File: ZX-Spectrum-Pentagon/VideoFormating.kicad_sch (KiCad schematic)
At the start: 10 parts

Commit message: annotate
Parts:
- gave numbers to parts that had none: 10
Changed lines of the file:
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@@
   (symbol (lib_id "74IEC:74HC574") (at 55.88 38.1 0) (unit 1)
     (in_bom yes) (on_board yes)
-    (property "Reference" "U?" (id 0) (at 55.88 24.13 0))
+    (property "Reference" "U36" (id 0) (at 55.88 24.13 0))
     (property "Value" "74HC574" (id 1) (at 55.88 52.07 0))
     (property "Footprint" "Package_DIP:DIP-20_W7.62mm" (id 2) (at 55.88 45.72 0)
@@
   (symbol (lib_id "74IEC:74HC574") (at 78.74 40.64 0) (unit 1)
     (in_bom yes) (on_board yes)
-    (property "Reference" "U?" (id 0) (at 78.74 26.67 0))
+    (property "Reference" "U37" (id 0) (at 78.74 26.67 0))
     (property "Value" "74HC574" (id 1) (at 78.74 54.61 0))
     (property "Footprint" "Package_DIP:DIP-20_W7.62mm" (id 2) (at 78.74 48.26 0)
@@
   (symbol (lib_id "power:GND") (at 68.58 57.15 0) (unit 1)
     (in_bom yes) (on_board yes)
-    (property "Reference" "#PWR?" (id 0) (at 68.58 63.5 0)
+    (property "Reference" "#PWR053" (id 0) (at 68.58 63.5 0)
       (effects (font (size 1.27 1.27)) hide)
     )
@@
   (symbol (lib_id "74IEC:74HC574") (at 55.88 167.64 0) (unit 1)
     (in_bom yes) (on_board yes)
-    (property "Reference" "U?" (id 0) (at 55.88 153.67 0))
+    (property "Reference" "U41" (id 0) (at 55.88 153.67 0))
     (property "Value" "74HC574" (id 1) (at 55.88 181.61 0))
     (property "Footprint" "Package_DIP:DIP-20_W7.62mm" (id 2) (at 55.88 175.26 0)
@@
   (symbol (lib_id "74IEC:74HC166") (at 82.55 168.91 0) (unit 1)
     (in_bom yes) (on_board yes)
-    (property "Reference" "U?" (id 0) (at 82.55 151.13 0))
+    (property "Reference" "U42" (id 0) (at 82.55 151.13 0))
     (property "Value" "74HC166" (id 1) (at 82.55 186.69 0))
     (property "Footprint" "Package_DIP:DIP-16_W7.62mm" (id 2) (at 82.55 184.15 0)
@@
   (symbol (lib_id "power:GND") (at 71.12 186.69 0) (unit 1)
     (in_bom yes) (on_board yes)
-    (property "Reference" "#PWR?" (id 0) (at 71.12 193.04 0)
+    (property "Reference" "#PWR057" (id 0) (at 71.12 193.04 0)
       (effects (font (size 1.27 1.27)) hide)
     )
@@
   (symbol (lib_id "74IEC:74XX153") (at 135.89 43.18 0) (unit 1)
     (in_bom yes) (on_board yes)
-    (property "Reference" "U?" (id 0) (at 135.89 26.67 0))
+    (property "Reference" "U38" (id 0) (at 135.89 26.67 0))
     (property "Value" "74HC153" (id 1) (at 135.89 59.69 0))
     (property "Footprint" "Package_DIP:DIP-16_W7.62mm" (id 2) (at 135.89 41.91 0)
@@
   (symbol (lib_id "74IEC:74XX153") (at 135.89 88.9 0) (unit 1)
     (in_bom yes) (on_board yes)
-    (property "Reference" "U?" (id 0) (at 135.89 72.39 0))
+    (property "Reference" "U39" (id 0) (at 135.89 72.39 0))
     (property "Value" "74HC153" (id 1) (at 135.89 105.41 0))
     (property "Footprint" "Package_DIP:DIP-16_W7.62mm" (id 2) (at 135.89 87.63 0)
@@
   (symbol (lib_id "power:GND") (at 124.46 125.73 0) (unit 1)
     (in_bom yes) (on_board yes)
-    (property "Reference" "#PWR?" (id 0) (at 124.46 132.08 0)
+    (property "Reference" "#PWR055" (id 0) (at 124.46 132.08 0)
       (effects (font (size 1.27 1.27)) hide)
     )
@@
   (symbol (lib_id "Gal:GAL16V8") (at 83.82 109.22 0) (unit 1)
     (in_bom yes) (on_board yes)
-    (property "Reference" "U?" (id 0) (at 83.82 95.25 0))
+    (property "Reference" "U40" (id 0) (at 83.82 95.25 0))
     (property "Value" "GAL16V8" (id 1) (at 83.82 123.19 0))
     (property "Footprint" "Package_DIP:DIP-20_W7.62mm" (id 2) (at 83.82 95.25 0)
@@
   (symbol (lib_id "zx_custom_symbol:SW_Push_DPDT") (at 114.3 166.37 0) (unit 1)
     (in_bom yes) (on_board yes)
-    (property "Reference" "SWVF?" (id 0) (at 114.3 153.67 0))
+    (property "Reference" "SWVF1" (id 0) (at 114.3 153.67 0))
     (property "Value" "128K/512K" (id 1) (at 114.3 184.15 0))
     (property "Footprint" "ZX-Spectrum-Pentagon:PS-22F03" (id 2) (at 114.3 166.37 0)
@@
   (symbol (lib_id "power:GND") (at 123.19 187.96 0) (mirror y) (unit 1)
     (in_bom yes) (on_board yes)
-    (property "Reference" "#PWR?" (id 0) (at 123.19 194.31 0)
+    (property "Reference" "#PWR058" (id 0) (at 123.19 194.31 0)
       (effects (font (size 1.27 1.27)) hide)
     )
@@
   (symbol (lib_id "Device:R") (at 106.68 153.67 0) (unit 1)
     (in_bom yes) (on_board yes)
-    (property "Reference" "RVF?" (id 0) (at 99.06 151.13 0)
+    (property "Reference" "RVF1" (id 0) (at 99.06 151.13 0)
       (effects (font (size 1.27 1.27)) (justify left))
     )
@@
   (symbol (lib_id "power:VCC") (at 106.68 144.78 0) (unit 1)
     (in_bom yes) (on_board yes)
-    (property "Reference" "#PWR?" (id 0) (at 106.68 148.59 0)
+    (property "Reference" "#PWR056" (id 0) (at 106.68 148.59 0)
       (effects (font (size 1.27 1.27)) hide)
     )
@@
   (symbol (lib_id "74IEC:74HC86") (at 137.16 137.16 0) (unit 4)
     (in_bom yes) (on_board yes)
-    (property "Reference" "U?" (id 0) (at 137.16 133.35 0))
+    (property "Reference" "U9" (id 0) (at 137.16 133.35 0))
     (property "Value" "74HC86" (id 1) (at 137.16 140.97 0))
     (property "Footprint" "Package_DIP:DIP-14_W7.62mm" (id 2) (at 137.16 144.78 0)
@@
   (symbol (lib_id "power:VCC") (at 67.31 120.65 90) (unit 1)
     (in_bom yes) (on_board yes)
-    (property "Reference" "#PWR?" (id 0) (at 71.12 120.65 0)
-      (effects (font (size 1.27 1.27)) hide)
-    )
+    (property "Reference" "#PWR054" (id 0) (at 71.12 120.65 0)
+      (effects (font (size 1.27 1.27)) hide)
+    )

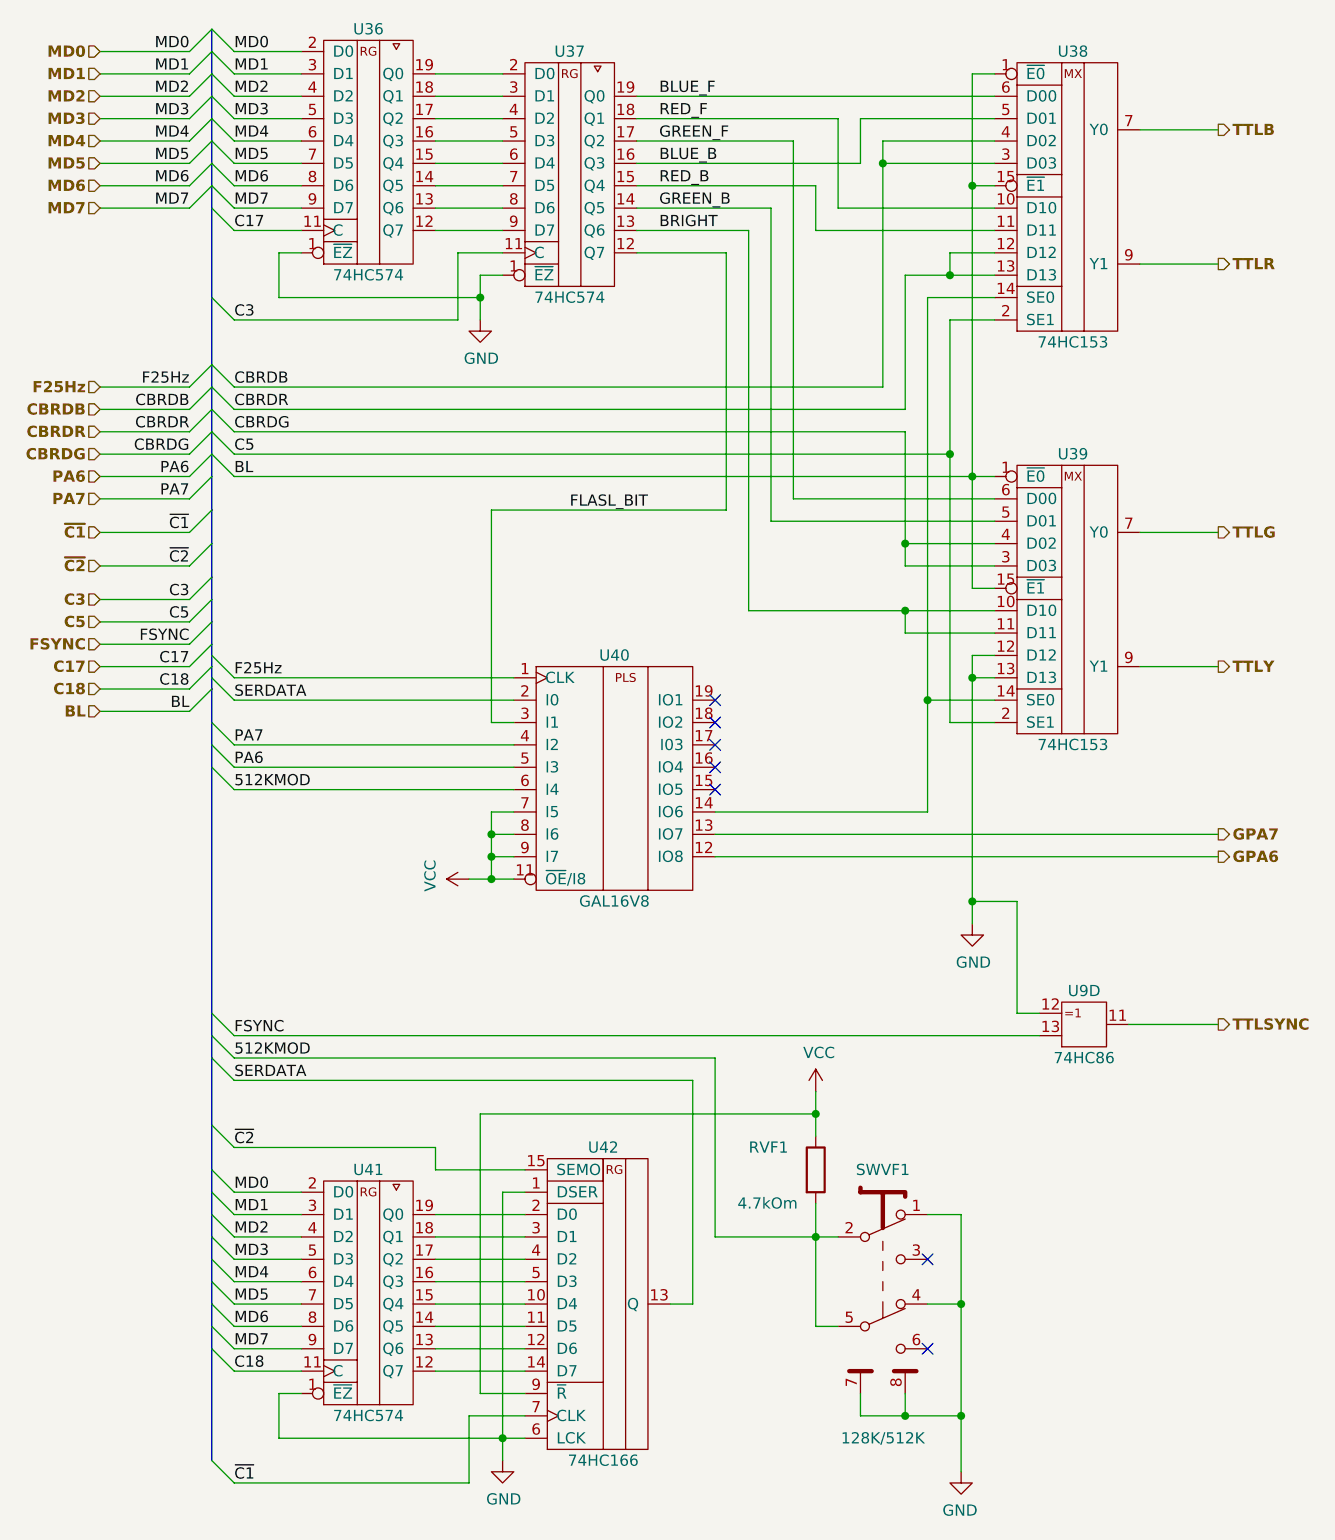
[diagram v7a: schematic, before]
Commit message: delete unuser labels fix problem with units
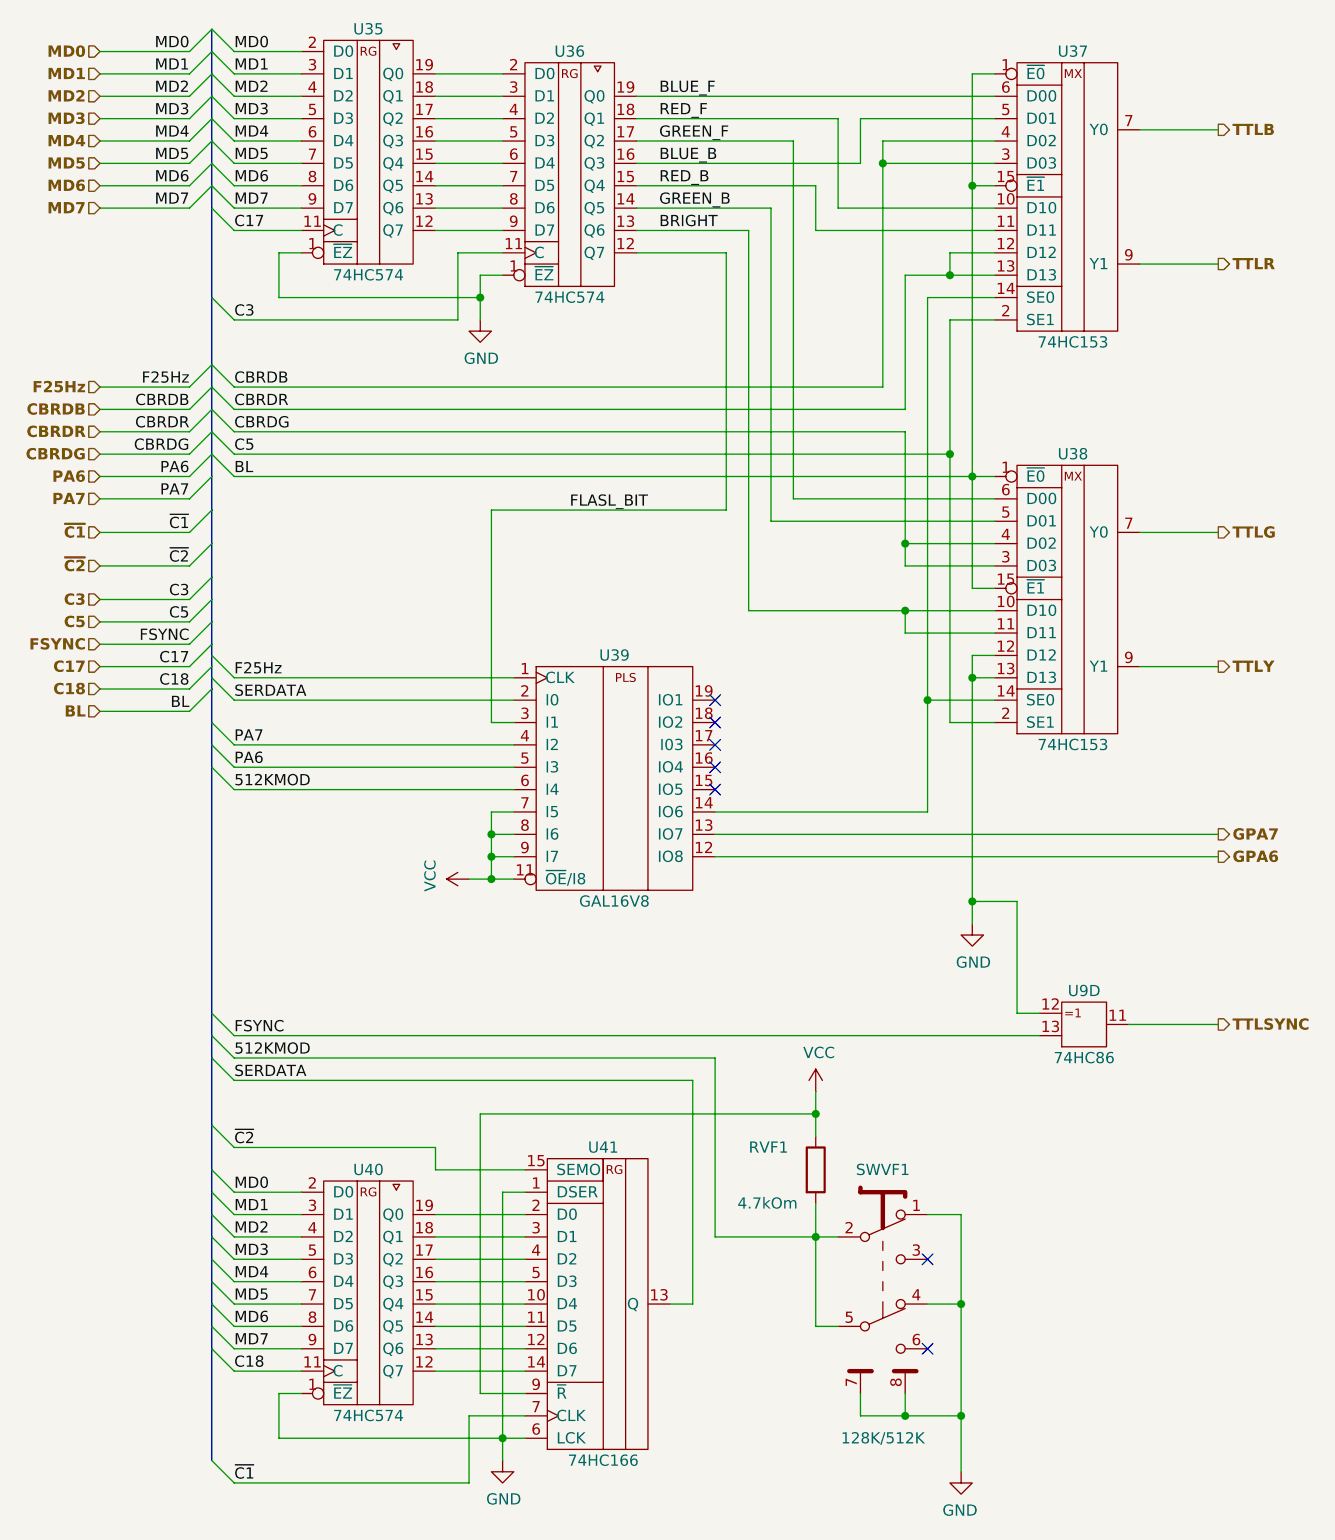
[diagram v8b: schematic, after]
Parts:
- renumbered U36 to U35, U37 to U36, U38 to U37, U39 to U38, U40 to U39, U41 to U40, U42 to U41
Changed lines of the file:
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@@
   (symbol (lib_id "74IEC:74HC574") (at 55.88 38.1 0) (unit 1)
     (in_bom yes) (on_board yes)
-    (property "Reference" "U36" (id 0) (at 55.88 24.13 0))
+    (property "Reference" "U35" (id 0) (at 55.88 24.13 0))
     (property "Value" "74HC574" (id 1) (at 55.88 52.07 0))
     (property "Footprint" "Package_DIP:DIP-20_W7.62mm" (id 2) (at 55.88 45.72 0)
@@
   (symbol (lib_id "74IEC:74HC574") (at 78.74 40.64 0) (unit 1)
     (in_bom yes) (on_board yes)
-    (property "Reference" "U37" (id 0) (at 78.74 26.67 0))
+    (property "Reference" "U36" (id 0) (at 78.74 26.67 0))
     (property "Value" "74HC574" (id 1) (at 78.74 54.61 0))
     (property "Footprint" "Package_DIP:DIP-20_W7.62mm" (id 2) (at 78.74 48.26 0)
@@
   (symbol (lib_id "74IEC:74HC574") (at 55.88 167.64 0) (unit 1)
     (in_bom yes) (on_board yes)
-    (property "Reference" "U41" (id 0) (at 55.88 153.67 0))
+    (property "Reference" "U40" (id 0) (at 55.88 153.67 0))
     (property "Value" "74HC574" (id 1) (at 55.88 181.61 0))
     (property "Footprint" "Package_DIP:DIP-20_W7.62mm" (id 2) (at 55.88 175.26 0)
@@
   (symbol (lib_id "74IEC:74HC166") (at 82.55 168.91 0) (unit 1)
     (in_bom yes) (on_board yes)
-    (property "Reference" "U42" (id 0) (at 82.55 151.13 0))
+    (property "Reference" "U41" (id 0) (at 82.55 151.13 0))
     (property "Value" "74HC166" (id 1) (at 82.55 186.69 0))
     (property "Footprint" "Package_DIP:DIP-16_W7.62mm" (id 2) (at 82.55 184.15 0)
@@
   (symbol (lib_id "74IEC:74XX153") (at 135.89 43.18 0) (unit 1)
     (in_bom yes) (on_board yes)
-    (property "Reference" "U38" (id 0) (at 135.89 26.67 0))
+    (property "Reference" "U37" (id 0) (at 135.89 26.67 0))
     (property "Value" "74HC153" (id 1) (at 135.89 59.69 0))
     (property "Footprint" "Package_DIP:DIP-16_W7.62mm" (id 2) (at 135.89 41.91 0)
@@
   (symbol (lib_id "74IEC:74XX153") (at 135.89 88.9 0) (unit 1)
     (in_bom yes) (on_board yes)
-    (property "Reference" "U39" (id 0) (at 135.89 72.39 0))
+    (property "Reference" "U38" (id 0) (at 135.89 72.39 0))
     (property "Value" "74HC153" (id 1) (at 135.89 105.41 0))
     (property "Footprint" "Package_DIP:DIP-16_W7.62mm" (id 2) (at 135.89 87.63 0)
@@
   (symbol (lib_id "Gal:GAL16V8") (at 83.82 109.22 0) (unit 1)
     (in_bom yes) (on_board yes)
-    (property "Reference" "U40" (id 0) (at 83.82 95.25 0))
+    (property "Reference" "U39" (id 0) (at 83.82 95.25 0))
     (property "Value" "GAL16V8" (id 1) (at 83.82 123.19 0))
     (property "Footprint" "Package_DIP:DIP-20_W7.62mm" (id 2) (at 83.82 95.25 0)
